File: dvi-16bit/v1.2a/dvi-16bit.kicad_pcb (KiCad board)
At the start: 4 copper layers, 40 x 40.8 mm, 39 parts, among them J1 PMOD, J10 sj, J2 PMOD, J3 jmp, J4 5V, J5 3v3_5v_sel, J6 HDMI_A_1.4, J7 sj, J8 sj, J9 sj, U1 VREG_3V3, U2 SII164

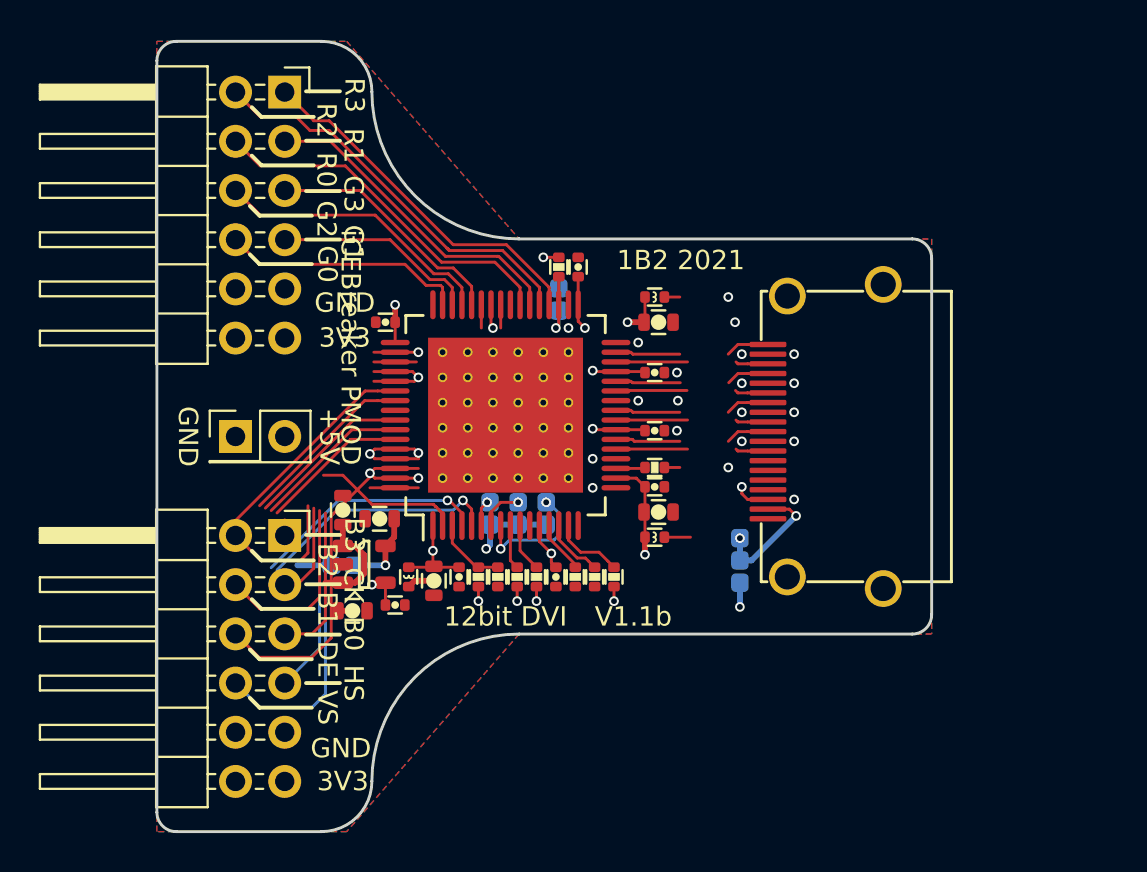
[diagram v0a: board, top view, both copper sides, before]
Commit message: assigned RGB565, moved U2 somewhat and started to re-route
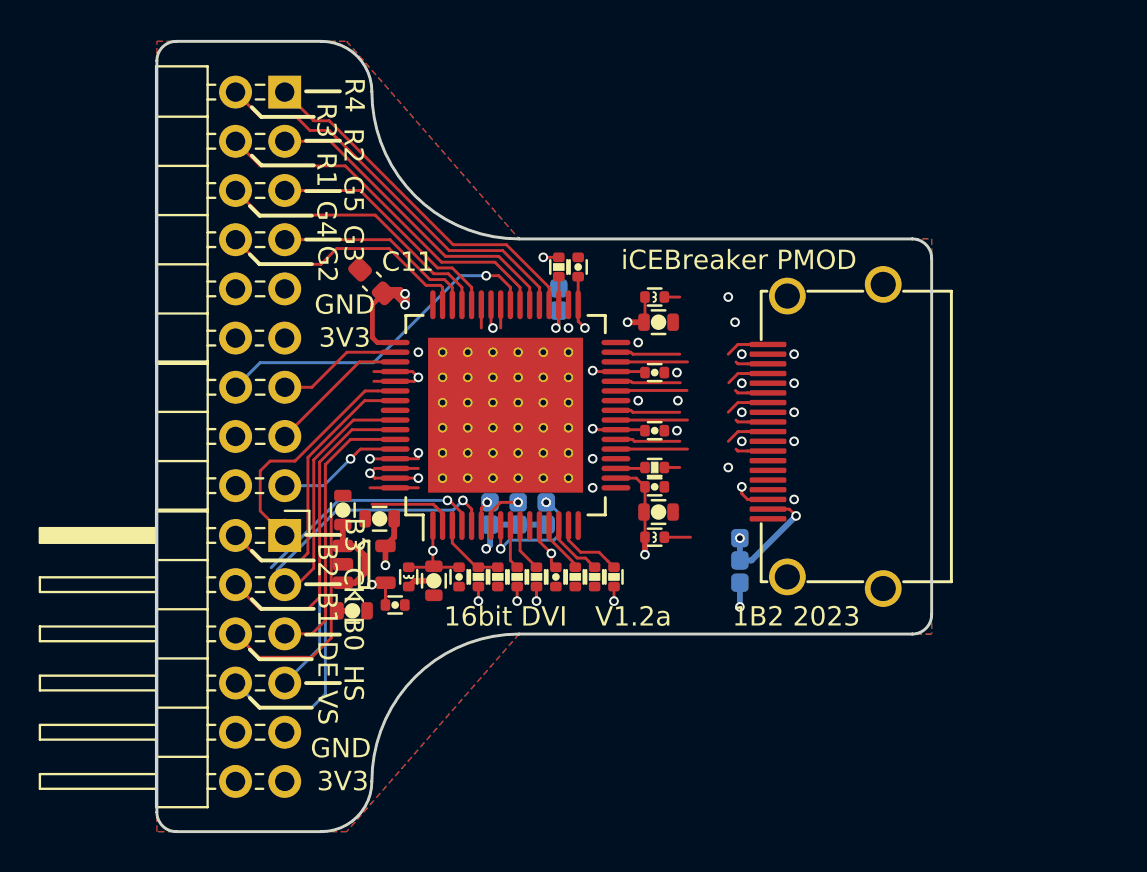
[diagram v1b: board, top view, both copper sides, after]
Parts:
- removed J3: jmp, pkl_jumpers:J_NC_0603_30
- C11: footprint pkl_dipol:C_0402 -> Capacitor_SMD:C_0603_1608Metric_Pad1.08x0.95mm_HandSolder
- J4: value 5V -> Conn_02x03_Odd_Even; footprint Connector_PinHeader_2.54mm:PinHeader_2x01_P2.54mm_Vertical -> Connector_PinHeader_2.54mm:PinHeader_2x03_P2.54mm_Horizontal
- moved J4 3.59 mm to (36.6, 42.7), turned to 180 degrees
- moved C11 2.21 mm to (41.1, 32.2), turned to 135 degrees
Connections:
- J1 pad 1: /B3 -> /B4
- J1 pad 12: Net-(J1-Pad12) -> +3V3
- J1 pad 3: /B0 -> /B1
- J1 pad 6: Net-(J1-Pad12) -> +3V3
- J1 pad 7: /B2 -> /B3
- J1 pad 8: /B1 -> /B2
- J2 pad 1: /R3 -> /R4
- J2 pad 10: /G0 -> /G2
- J2 pad 12: Net-(J1-Pad12) -> +3V3
- J2 pad 2: /R1 -> /R2
- J2 pad 3: /G3 -> /G5
- J2 pad 4: /G1 -> /G3
- J2 pad 6: Net-(J1-Pad12) -> +3V3
- J2 pad 7: /R2 -> /R3
- J2 pad 8: /R0 -> /R1
- J2 pad 9: /G2 -> /G4
- J4 pad 1: GND -> /B0
- J4 pad 2: +5V -> GND
- J6 pad 13: (no net) -> Net-(J6-Pad13)
- J6 pad 14: (no net) -> Net-(J6-Pad14)
- J6 pad 15: (no net) -> Net-(J6-Pad15)
- J6 pad 16: (no net) -> Net-(J6-Pad16)
- J6 pad 19: (no net) -> Net-(J6-Pad19)
- U2 pad 11: (no net) -> Net-(U2-Pad11)
- U2 pad 36: /R3 -> /R4
- U2 pad 37: /R2 -> /R3
- U2 pad 38: /R1 -> /R2
- U2 pad 39: /R0 -> /R1
- U2 pad 40: GND -> /R0
- U2 pad 44: /G3 -> /G5
- U2 pad 45: /G2 -> /G4
- U2 pad 46: /G1 -> /G3
- U2 pad 47: /G0 -> /G2
- U2 pad 50: GND -> /G1
- U2 pad 51: GND -> /G0
- U2 pad 54: /B3 -> /B4
- U2 pad 55: /B2 -> /B3
- U2 pad 58: /B1 -> /B2
- U2 pad 59: /B0 -> /B1
- U2 pad 60: GND -> /B0
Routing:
- net /R4: track 0.00 -> 18.7 mm
- net /G4: track 0.00 -> 14.7 mm
- net /B4: track 0.00 -> 13.3 mm
- net /G5: track 0.00 -> 12.6 mm
- net +5V: track 37.3 -> 25.5 mm, vias 2 -> 1
- net /B0: track 15.6 -> 6.48 mm, vias 0 -> 1
- net /PVCC: track 32.8 -> 41.8 mm, vias 2 -> 3
- net GND: track 28.1 -> 20.8 mm
- net /DE: track 22.7 -> 16.6 mm
- net /G0: track 12.6 -> 7.29 mm
- net /R2: track 21.1 -> 16.7 mm
- net Net-(J4-Pad3): track 0.00 -> 4.34 mm, vias 0 -> 1
- net /G1: track 10.6 -> 6.45 mm
- net /B3: track 11.8 -> 15.1 mm
- net /B1: track 17.7 -> 14.6 mm
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- added copper zone on VCC.Cu, net +3V3
- added copper zone on GND.Cu, net GND
- removed copper zone on In1.Cu, net +3V3
- removed copper zone on In2.Cu, net GND
- removed copper zone on In1.Cu, net Net-(J1-Pad12)
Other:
- board text added: "16bit DVI"
- board text added: "1B2 2023"
- board text added: "C11"
- board text added: "G4"
- board text added: "G5"
- board text added: "R4"
- board text added: "V1.2a"
- board text removed: "12bit DVI"
- board text removed: "1B2 2021"

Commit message: more routing and silkscreen fixes
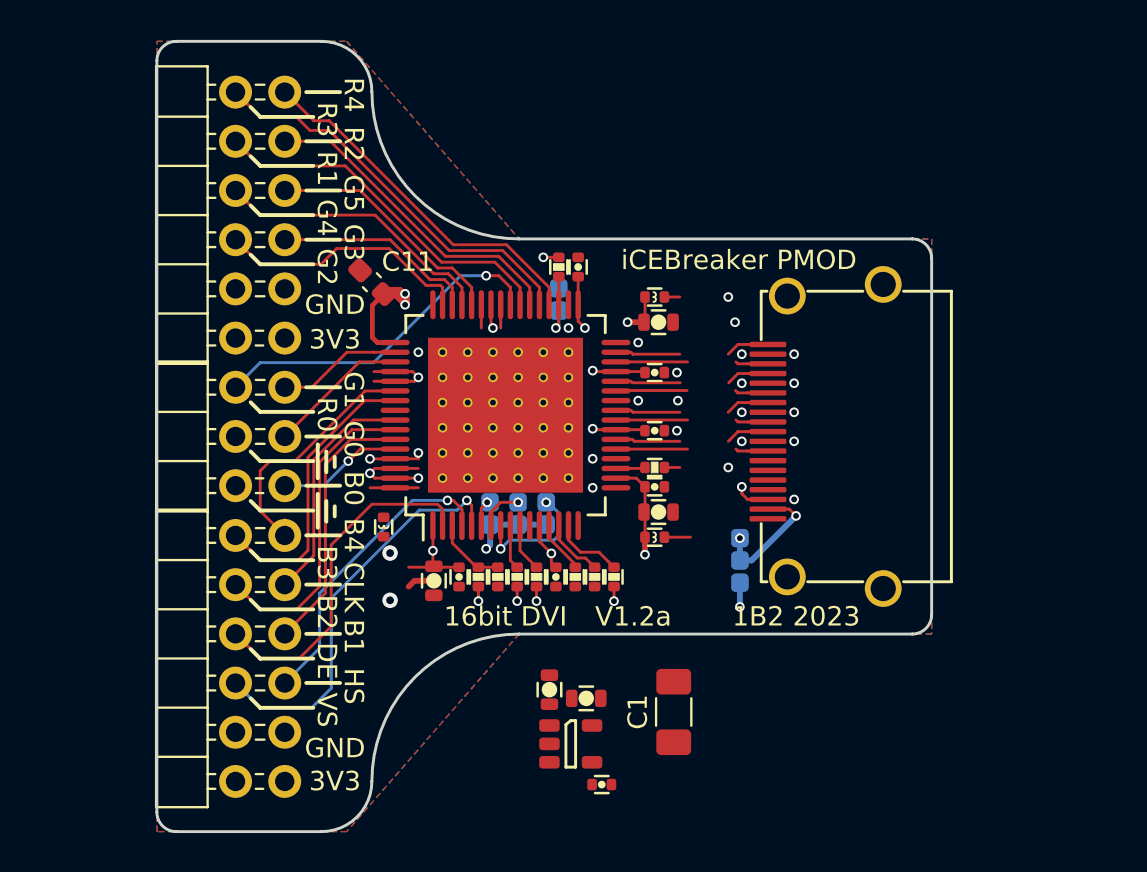
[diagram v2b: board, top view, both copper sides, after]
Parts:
- C1: footprint pkl_dipol:C_0603 -> Capacitor_SMD:C_1206_3216Metric_Pad1.33x1.80mm_HandSolder
- moved C1 17.4 mm to (56.7, 54.4), turned to 90 degrees
- moved C3 14.1 mm to (53.0, 58.2)
- moved C2 14.1 mm to (50.3, 53.3)
- moved U1 14.1 mm to (51.4, 56.1)
- moved C4 14.1 mm to (52.2, 53.7)
- moved L1 2.88 mm to (41.7, 44.9)
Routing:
- net +5V: track 25.5 -> 19.9 mm
- net GND: track 20.8 -> 25.3 mm
- net /VS: track 24.4 -> 21.0 mm
- net +3V3: track 15.8 -> 12.4 mm
- net /DE: track 16.6 -> 17.9 mm
- net Net-(C3-Pad1): track 1.15 -> 0.00 mm
- net /B1: track 14.6 -> 13.7 mm
- net Net-(J4-Pad3): track 4.34 -> 4.20 mm, vias 1 -> 0
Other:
- board text added: "B4"
- board text added: "CLK"

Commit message: more routing and placing
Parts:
- C10, C6: footprint pkl_dipol:C_0402 -> Capacitor_SMD:C_0603_1608Metric_Pad1.08x0.95mm_HandSolder
- J10: value sj -> Jumper_NO_Small; footprint pkl_jumpers:J_0603 -> Connector_PinHeader_2.00mm:PinHeader_1x02_P2.00mm_Vertical; moved to F.Cu
- R3: footprint pkl_dipol:R_0402 -> Resistor_SMD:R_0603_1608Metric_Pad0.98x0.95mm_HandSolder
- moved J10 7.31 mm to (57.8, 31.3)
- moved C6 3.27 mm to (54.9, 32.3), turned to 45 degrees
- moved L3 1.94 mm to (57.6, 33.2)
- moved C1 1.75 mm to (58.0, 55.6)
- moved C16 1.39 mm to (57.3, 34.6)
- moved C10 1.16 mm to (56.9, 36.8)
- moved R3 0.69 mm to (51.2, 31.0), turned to 0 degrees
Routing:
- net /DKEN: track 3.67 -> 9.36 mm, vias 1 -> 0
- net GND: track 25.3 -> 20.8 mm
- net Net-(J4-Pad3): track 4.20 -> 0.00 mm
- net /VCC: track 35.6 -> 39.6 mm
- net /D2-: track 5.39 -> 8.22 mm
- net /D0-: track 5.39 -> 8.22 mm
- net /D1-: track 5.41 -> 8.22 mm
- net /HS: track 18.4 -> 15.8 mm
- net /D1+: track 5.58 -> 8.22 mm
- net /D0+: track 5.60 -> 8.22 mm
- net /D2+: track 5.60 -> 8.22 mm
- net /TVDD: track 14.3 -> 12.0 mm
- net +3V3: track 12.4 -> 12.0 mm, vias 12 -> 10
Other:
- board text added: "iCEBreaker"
- board text removed: "iCEBreaker PMOD"

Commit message: more routing and placing
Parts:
- C15: footprint pkl_dipol:C_0603 -> Capacitor_SMD:C_0805_2012Metric_Pad1.18x1.45mm_HandSolder
- C7, C9: footprint pkl_dipol:C_0402 -> Capacitor_SMD:C_0603_1608Metric_Pad1.08x0.95mm_HandSolder
- L2: footprint pkl_dipol:L_0402 -> Inductor_SMD:L_0603_1608Metric_Pad1.05x0.95mm_HandSolder
- R9: footprint pkl_dipol:R_0402 -> Resistor_SMD:R_0603_1608Metric_Pad0.98x0.95mm_HandSolder
- moved L2 1.75 mm to (56.9, 46.7), turned to 0 degrees
- moved C15 1.49 mm to (57.1, 45.0)
- moved C9 1.25 mm to (56.9, 43.3)
- moved C7 1.16 mm to (56.9, 39.8)
- moved R9 1.15 mm to (56.9, 41.9)
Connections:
- J4 pad 2: GND -> /G0
- J4 pad 3: /G0 -> +5V
- L2 pad 1: +3V3 -> /PVCC
- L2 pad 2: /PVCC -> +3V3
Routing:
- net +5V: track 19.9 -> 30.9 mm
- net /PVCC: track 41.8 -> 49.3 mm, vias 3 -> 4
- net /G0: track 7.29 -> 11.9 mm
- net /CK-: track 5.39 -> 9.78 mm
- net /CK+: track 5.60 -> 8.22 mm
- net +3V3: track 12.0 -> 14.3 mm, vias 10 -> 12
- net /B4: track 13.3 -> 11.3 mm
- net /TVDD: track 12.0 -> 12.7 mm
- net /TFADJ: track 1.52 -> 2.24 mm
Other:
- board text added: "5V"
- board text added: "C10"
- board text added: "C15"
- board text added: "C7"
- board text added: "C9"
- board text added: "R9"

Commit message: more routing and fixes
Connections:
- J4 pad 5: /G1 -> /R0
- J4 pad 6: /R0 -> /G1
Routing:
- net +3V3: track 14.3 -> 18.3 mm
- net /PVCC: track 49.3 -> 45.4 mm
- net /G1: track 6.45 -> 8.99 mm
- net /R0: track 17.7 -> 15.2 mm
- net /VCC: track 39.6 -> 38.4 mm
- added copper zone on 3V3.Cu, net +3V3
- removed copper zone on VCC.Cu, net +3V3

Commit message: more routing and fixes
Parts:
- removed C15: 10u, Capacitor_SMD:C_0805_2012Metric_Pad1.18x1.45mm_HandSolder
- removed the C3 at (53.0, 58.2)
- removed the C5 at (50.6, 47.5)
- removed the C8 at (45.6, 47.5)
- removed the R1 at (53.6, 47.5)
- removed R2, R4, R8: 10k, pkl_dipol:R_0402
- removed U1: VREG_3V3, pkl_housings_sot:SOT-23-5
- added C11: 10u, Capacitor_SMD:C_0805_2012Metric_Pad1.18x1.45mm_HandSolder, F.Cu at (57.9, 45.0)
- added RN1: R_Pack04, dvi-16bit:RESCAF80P320X160X60-8N, F.Cu at (53.7, 48.3)
- C10: renamed from C14; footprint pkl_dipol:C_0603 -> Capacitor_SMD:C_0805_2012Metric_Pad1.18x1.45mm_HandSolder
- C2, C4: value 4u7 -> 100n; footprint pkl_dipol:C_0603 -> Capacitor_SMD:C_0603_1608Metric_Pad1.08x0.95mm_HandSolder
- C9: renamed from C16; footprint pkl_dipol:C_0603 -> Capacitor_SMD:C_0805_2012Metric
- L1, L3: footprint pkl_dipol:L_0402 -> Inductor_SMD:L_0603_1608Metric_Pad1.05x0.95mm_HandSolder
- R5, R6, R7: footprint pkl_dipol:R_0402 -> Resistor_SMD:R_0603_1608Metric_Pad0.98x0.95mm_HandSolder
- moved C1 16.9 mm to (42.0, 50.0), turned to 270 degrees
- moved C4 8.35 mm to (45.9, 48.2), turned to 270 degrees
- moved R7 6.59 mm to (58.0, 49.1), turned to 0 degrees
- moved C2 5.07 mm to (50.3, 48.2), turned to 270 degrees
- moved R5 2.33 mm to (48.8, 48.2)
- moved C10 1.75 mm to (44.2, 49.4)
- moved L1 1.28 mm to (41.1, 46.0), turned to 225 degrees
- moved L2 1.13 mm to (58.0, 46.7)
- moved C9 0.98 mm to (58.2, 34.4)
- moved R6 0.79 mm to (47.4, 48.2)
- moved L3 0.77 mm to (58.3, 32.7), turned to 0 degrees
- moved J10 0.37 mm to (57.6, 31.1)
- renumbered C6 to C3, C11 to C5, C9 to C6, C10 to C8, R3 to R1
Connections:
- C1 pad 1: +3V3 -> +5V
- C2 pad 1: +5V -> /VCC
- C4 pad 1: +3V3 -> /VCC
- L1 pad 1: +3V3 -> /VCC
- L1 pad 2: /VCC -> +3V3
- L3 pad 1: +3V3 -> /TVDD
- L3 pad 2: /TVDD -> +3V3
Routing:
- net +3V3: track 18.3 -> 31.9 mm, vias 12 -> 7
- net /VCC: track 38.4 -> 50.9 mm, vias 3 -> 5
- net /ISEL-~RST: track 2.71 -> 12.2 mm
- net /EDGE-HTPLG: track 2.29 -> 10.7 mm
- net /~PD: track 2.50 -> 9.40 mm
- net /PVCC: track 45.4 -> 51.3 mm
- net /TVDD: track 12.7 -> 18.0 mm, vias 3 -> 4
- net +5V: track 30.9 -> 35.2 mm, vias 1 -> 3
- net /VREF: track 3.77 -> 5.26 mm
- net /DK2: track 2.31 -> 1.20 mm
- net /DSEL-SDA: track 3.17 -> 3.77 mm
- net /DK1: track 6.56 -> 6.07 mm, vias 2 -> 1
- net GND: vias 26 -> 27
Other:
- board text added: "C5"
- board text removed: "C15"
- board text removed: "CLK"

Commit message: more fixes
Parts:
- moved J5 0.36 mm to (60.1, 46.2)
- renumbered R5 to R2, R6 to R3, R7 to R4, R9 to R5
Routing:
- net +3V3: track 31.9 -> 32.8 mm, vias 7 -> 8
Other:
- board text added: "C1"
- board text added: "C2"
- board text added: "C3"
- board text added: "C4"
- board text added: "C6"
- board text added: "C8"
- board text added: "L1"
- board text added: "L2"
- board text added: "L3"
- board text added: "R5"
- board text removed: "R9"

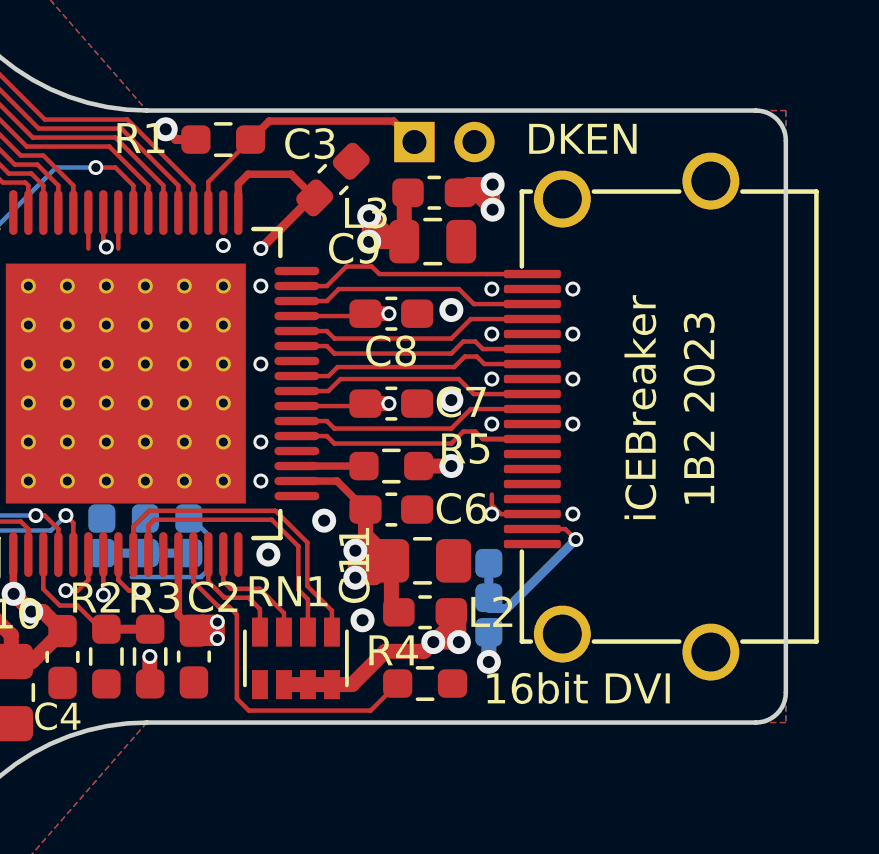
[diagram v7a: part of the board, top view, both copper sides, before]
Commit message: fixed 5V/3V3 solderjumper for HDMI pin 18, and some other small fixes
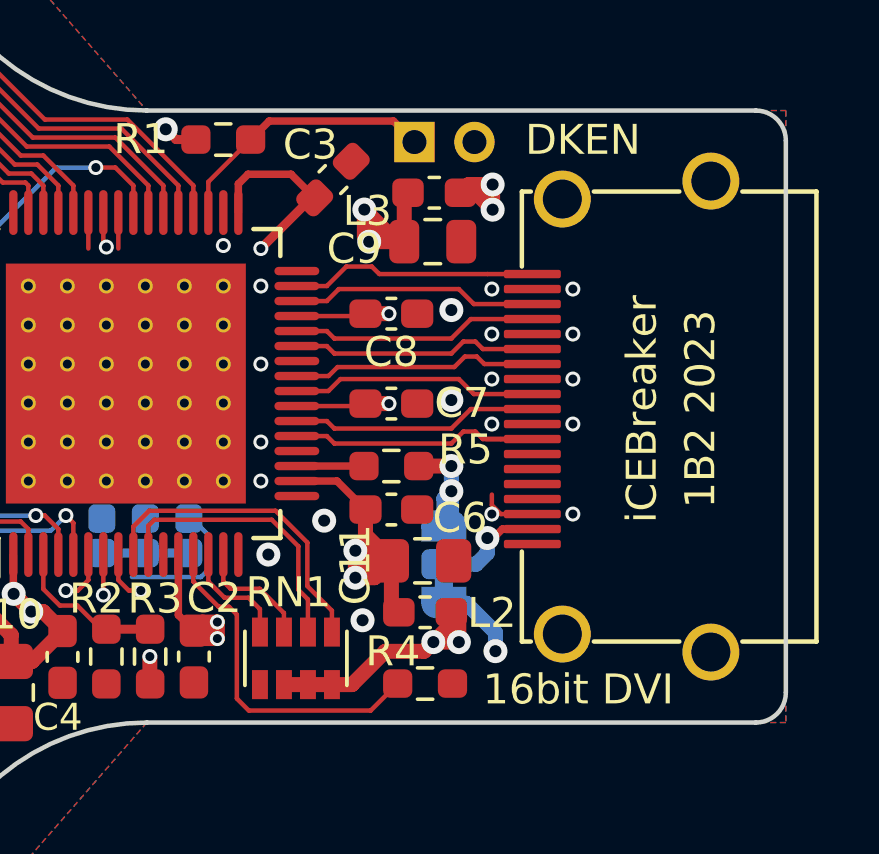
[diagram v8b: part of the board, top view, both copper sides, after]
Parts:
- J5: value 3v3_5v_sel -> SolderJumper_3_Bridged12; footprint pkl_jumpers:J_NCNO_0903_30 -> Jumper:SolderJumper-3_P1.3mm_Bridged12_RoundedPad1.0x1.5mm
- moved J5 1.87 mm to (58.6, 45.1), turned to 90 degrees
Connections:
- J5 pad 1: +3V3 -> +5V
- J5 pad 3: +5V -> +3V3
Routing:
- net /TVDD: track 18.0 -> 21.4 mm
- net +3V3: track 32.8 -> 36.1 mm, vias 8 -> 9
- net +5V: track 35.0 -> 37.1 mm
- net Net-(J5-Pad2): track 5.45 -> 3.73 mm
